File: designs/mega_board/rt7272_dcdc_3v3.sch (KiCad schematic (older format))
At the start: 14 parts, among them U2 RT7272

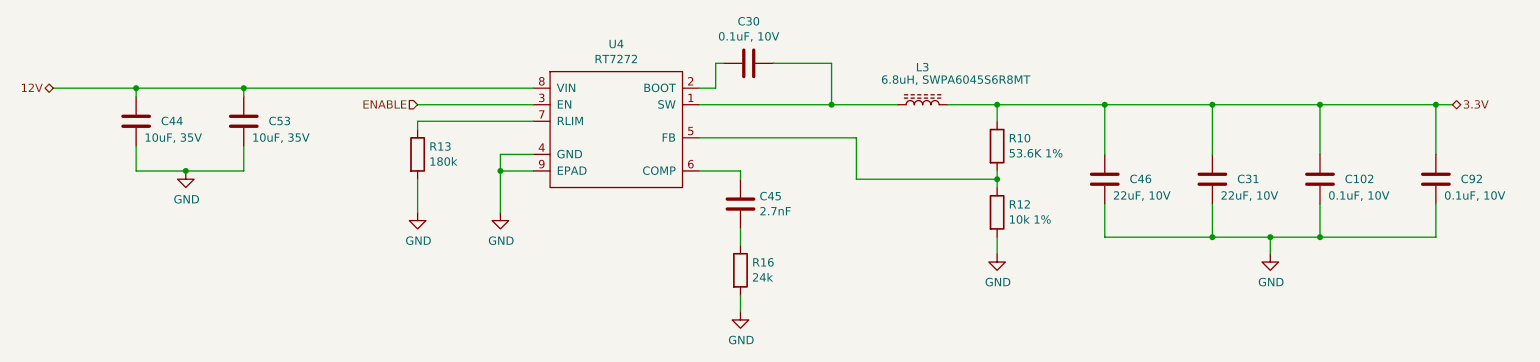
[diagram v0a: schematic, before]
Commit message: renamed net from +12V to VCC
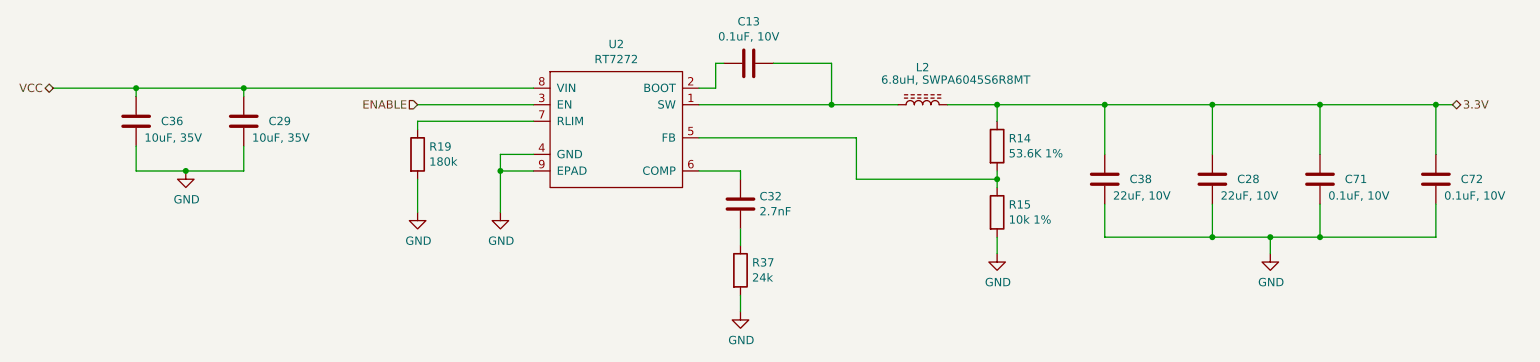
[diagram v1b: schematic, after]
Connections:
- net 12V renamed VCC
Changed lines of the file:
@@
 $Descr A4 11693 8268
 encoding utf-8
-Sheet 6 14
+Sheet 9 14
 Title ""
 Date ""
@@
 AR Path="/5D0328DE/5D42E225/5D42D1B4" Ref="U6"  Part="1"
 AR Path="/5D42D1B4" Ref="U?"  Part="1"
-F 0 "U4" H 5600 4015 50  0000 C CNN
+F 0 "U2" H 5600 4015 50  0000 C CNN
 F 1 "RT7272" H 5600 3924 50  0000 C CNN
 F 2 "LibreRouter_MegaBoard:RT8250-SOP8" H 5600 3500 50  0001 C CNN
@@
 AR Path="/5D0328DE/5D42CD47/5D42D229" Ref="C29"  Part="1"
 AR Path="/5D0328DE/5D42E225/5D42D229" Ref="C15"  Part="1"
-F 0 "C53" H 3500 3450 50  0000 L CNN
+F 0 "C29" H 3500 3450 50  0000 L CNN
 F 1 "10uF, 35V" H 3400 3350 50  0000 L CNN
 F 2 "LibreRouter_MegaBoard:C0805" H 3388 3300 50  0001 C CNN
@@
 AR Path="/5D0328DE/5D42CD47/5D42D2DE" Ref="R19"  Part="1"
 AR Path="/5D0328DE/5D42E225/5D42D2DE" Ref="R58"  Part="1"
-F 0 "R13" H 4470 3696 50  0000 L CNN
+F 0 "R19" H 4470 3696 50  0000 L CNN
 F 1 "180k" H 4470 3605 50  0000 L CNN
 F 2 "LibreRouter_MegaBoard:R0402" V 4330 3650 50  0001 C CNN
@@
 AR Path="/5D0328DE/5D42CD47/5D42D3B9" Ref="L2"  Part="1"
 AR Path="/5D0328DE/5D42E225/5D42D3B9" Ref="L8"  Part="1"
-F 0 "L3" V 7675 3350 50  0000 C CNN
+F 0 "L2" V 7675 3350 50  0000 C CNN
 F 1 "6.8uH, SWPA6045S6R8MT" V 7600 3150 50  0000 C CNN
 F 2 "LibreRouter_MegaBoard:SWPA6028S" H 7450 3350 50  0001 C CNN
@@
 AR Path="/5D0328DE/5D42CD47/5D42D488" Ref="C13"  Part="1"
 AR Path="/5D0328DE/5D42E225/5D42D488" Ref="C12"  Part="1"
-F 0 "C30" V 6148 3100 50  0000 C CNN
+F 0 "C13" V 6148 3100 50  0000 C CNN
 F 1 "0.1uF, 10V" V 6239 3100 50  0000 C CNN
 F 2 "LibreRouter_MegaBoard:C0402" H 6438 2950 50  0001 C CNN
@@
 AR Path="/5D0328DE/5D42CD47/5D42D571" Ref="R14"  Part="1"
 AR Path="/5D0328DE/5D42E225/5D42D571" Ref="R9"  Part="1"
-F 0 "R10" H 7970 3646 50  0000 L CNN
+F 0 "R14" H 7970 3646 50  0000 L CNN
 F 1 "53.6K 1%" H 7970 3555 50  0000 L CNN
 F 2 "LibreRouter_MegaBoard:R0402" V 7830 3600 50  0001 C CNN
@@
 AR Path="/5D0328DE/5D42CD47/5D42D5CB" Ref="R15"  Part="1"
 AR Path="/5D0328DE/5D42E225/5D42D5CB" Ref="R11"  Part="1"
-F 0 "R12" H 7970 4046 50  0000 L CNN
+F 0 "R15" H 7970 4046 50  0000 L CNN
 F 1 "10k 1%" H 7970 3955 50  0000 L CNN
 F 2 "LibreRouter_MegaBoard:R0402" V 7830 4000 50  0001 C CNN
@@
 AR Path="/5D0328DE/5D42CD47/5D42D605" Ref="R37"  Part="1"
 AR Path="/5D0328DE/5D42E225/5D42D605" Ref="R59"  Part="1"
-F 0 "R16" H 6420 4396 50  0000 L CNN
+F 0 "R37" H 6420 4396 50  0000 L CNN
 F 1 "24k" H 6420 4305 50  0000 L CNN
 F 2 "LibreRouter_MegaBoard:R0402" V 6280 4350 50  0001 C CNN
@@
 AR Path="/5D0328DE/5D42CD47/5D42D659" Ref="C32"  Part="1"
 AR Path="/5D0328DE/5D42E225/5D42D659" Ref="C16"  Part="1"
-F 0 "C45" H 6235 3904 50  0000 R CNN
+F 0 "C32" H 6235 3904 50  0000 R CNN
 F 1 "2.7nF" H 6235 3995 50  0000 R CNN
 F 2 "LibreRouter_MegaBoard:C0402" H 6388 3800 50  0001 C CNN
@@
 AR Path="/5D0328DE/5D42CD47/5D42DAC0" Ref="C38"  Part="1"
 AR Path="/5D0328DE/5D42E225/5D42DAC0" Ref="C17"  Part="1"
-F 0 "C46" H 8400 3800 50  0000 R CNN
+F 0 "C38" H 8400 3800 50  0000 R CNN
 F 1 "22uF, 10V" H 8500 3900 50  0000 R CNN
 F 2 "LibreRouter_MegaBoard:C0805" H 8588 3650 50  0001 C CNN
@@
 AR Path="/5D0328DE/5D42CD47/5D42DBCD" Ref="C28"  Part="1"
 AR Path="/5D0328DE/5D42E225/5D42DBCD" Ref="C14"  Part="1"
-F 0 "C31" H 9050 3800 50  0000 R CNN
+F 0 "C28" H 9050 3800 50  0000 R CNN
 F 1 "22uF, 10V" H 9150 3900 50  0000 R CNN
 F 2 "LibreRouter_MegaBoard:C0805" H 9238 3650 50  0001 C CNN
@@
 AR Path="/5D0328DE/5D42CD47/5D42DC2B" Ref="C71"  Part="1"
 AR Path="/5D0328DE/5D42E225/5D42DC2B" Ref="C91"  Part="1"
-F 0 "C102" H 9700 3800 50  0000 R CNN
+F 0 "C71" H 9700 3800 50  0000 R CNN
 F 1 "0.1uF, 10V" H 9800 3900 50  0000 R CNN
 F 2 "LibreRouter_MegaBoard:C0402" H 9888 3650 50  0001 C CNN
@@
 AR Path="/5D0328DE/5D42CD47/5D42DCB2" Ref="C72"  Part="1"
 AR Path="/5D0328DE/5D42E225/5D42DCB2" Ref="C92"  Part="1"
-F 0 "C92" H 10400 3800 50  0000 R CNN
+F 0 "C72" H 10400 3800 50  0000 R CNN
 F 1 "0.1uF, 10V" H 10500 3900 50  0000 R CNN
 F 2 "LibreRouter_MegaBoard:C0402" H 10588 3650 50  0001 C CNN
@@
 AR Path="/5D0328DE/5D42CD47/5D42DD90" Ref="#PWR0139"  Part="1"
 AR Path="/5D0328DE/5D42E225/5D42DD90" Ref="#PWR0145"  Part="1"
-F 0 "#PWR0145" H 7900 4000 50  0001 C CNN
+F 0 "#PWR0139" H 7900 4000 50  0001 C CNN
 F 1 "GND" H 7905 4077 50  0000 C CNN
 F 2 "" H 7900 4250 50  0001 C CNN
@@
 AR Path="/5D0328DE/5D42CD47/5D42DDBC" Ref="#PWR0140"  Part="1"
 AR Path="/5D0328DE/5D42E225/5D42DDBC" Ref="#PWR0146"  Part="1"
-F 0 "#PWR0146" H 9550 4000 50  0001 C CNN
+F 0 "#PWR0140" H 9550 4000 50  0001 C CNN
 F 1 "GND" H 9555 4077 50  0000 C CNN
 F 2 "" H 9550 4250 50  0001 C CNN
@@
 AR Path="/5D0328DE/5D42CD47/5D42FF27" Ref="#PWR0141"  Part="1"
 AR Path="/5D0328DE/5D42E225/5D42FF27" Ref="#PWR0147"  Part="1"
-F 0 "#PWR0147" H 6350 4350 50  0001 C CNN
+F 0 "#PWR0141" H 6350 4350 50  0001 C CNN
 F 1 "GND" H 6355 4427 50  0000 C CNN
 F 2 "" H 6350 4600 50  0001 C CNN
@@
 AR Path="/5D0328DE/5D42CD47/5D43058C" Ref="C36"  Part="1"
 AR Path="/5D0328DE/5D42E225/5D43058C" Ref="C19"  Part="1"
-F 0 "C44" H 2850 3450 50  0000 L CNN
+F 0 "C36" H 2850 3450 50  0000 L CNN
 F 1 "10uF, 35V" H 2750 3350 50  0000 L CNN
 F 2 "LibreRouter_MegaBoard:C0805" H 2738 3300 50  0001 C CNN
@@
 ENABLE
 Text HLabel 2200 3250 0    50   BiDi ~ 0
-12V
+VCC
 Text HLabel 10650 3350 2    50   BiDi ~ 0
 3.3V
@@
 AR Path="/5D0328DE/5D42CD47/5D4322E2" Ref="#PWR0142"  Part="1"
 AR Path="/5D0328DE/5D42E225/5D4322E2" Ref="#PWR0148"  Part="1"
-F 0 "#PWR0148" H 3000 3500 50  0001 C CNN
+F 0 "#PWR0142" H 3000 3500 50  0001 C CNN
 F 1 "GND" H 3005 3577 50  0000 C CNN
 F 2 "" H 3000 3750 50  0001 C CNN
@@
 AR Path="/5D0328DE/5D42CD47/5D4323C5" Ref="#PWR0143"  Part="1"
 AR Path="/5D0328DE/5D42E225/5D4323C5" Ref="#PWR0149"  Part="1"
-F 0 "#PWR0149" H 4400 3750 50  0001 C CNN
+F 0 "#PWR0143" H 4400 3750 50  0001 C CNN
 F 1 "GND" H 4405 3827 50  0000 C CNN
 F 2 "" H 4400 4000 50  0001 C CNN
@@
 AR Path="/5D0328DE/5D42CD47/5D4323EC" Ref="#PWR0144"  Part="1"
 AR Path="/5D0328DE/5D42E225/5D4323EC" Ref="#PWR0150"  Part="1"
-F 0 "#PWR0150" H 4900 3750 50  0001 C CNN
+F 0 "#PWR0144" H 4900 3750 50  0001 C CNN
 F 1 "GND" H 4905 3827 50  0000 C CNN
 F 2 "" H 4900 4000 50  0001 C CNN
